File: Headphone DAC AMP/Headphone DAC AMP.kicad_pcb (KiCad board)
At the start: 4 copper layers, 95 parts, among them J1 2137160001, J2 M50-3551042, J4 PINHD_1x2_Male, U1 NCV8187AMTW090TAG, U11 ADP5071AREZ-R7, U2 XU316-1024-QF60B-C24, U6 MCP1727-1802xSN, U7 MCP1727-3302xSN, U8 W25Q16JVSNIQ, Y1 Crystal_GND24, Y2 LMK6CE049152CDLFR, Y3 ASDLJ-E-45.1584MHz

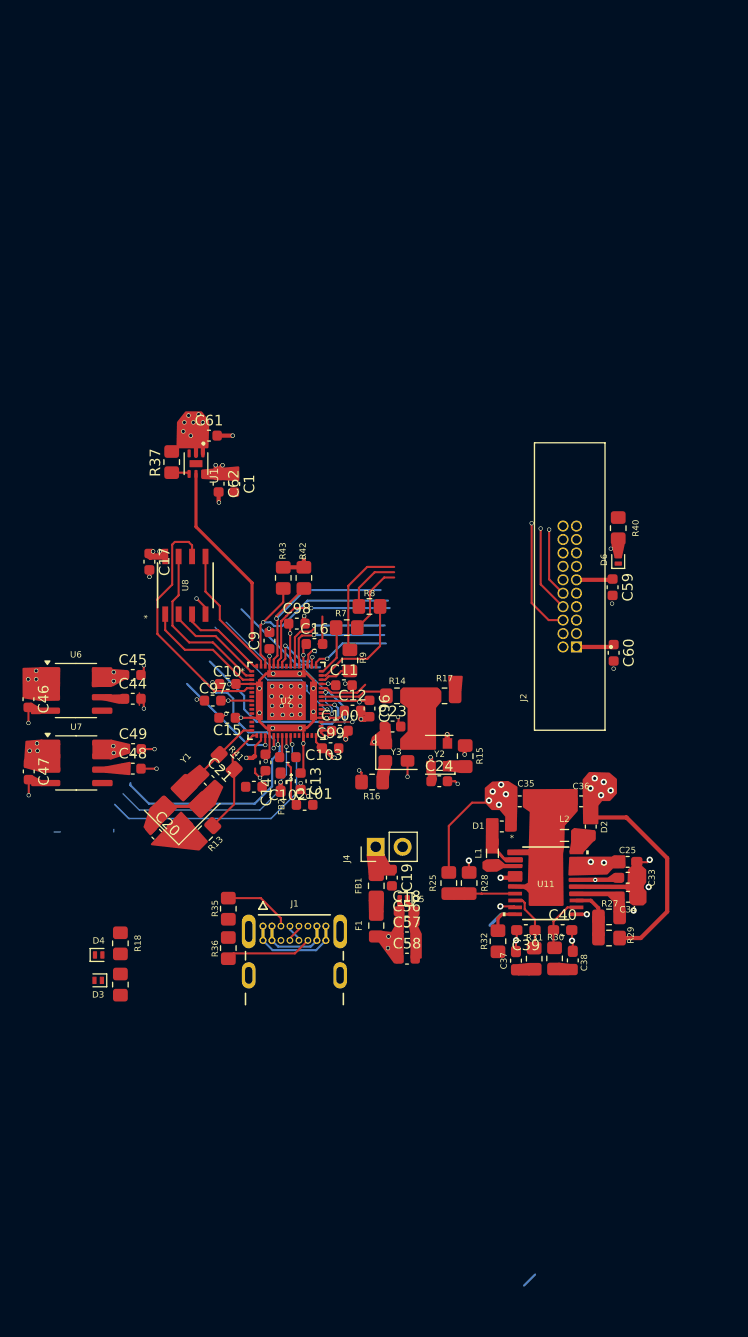
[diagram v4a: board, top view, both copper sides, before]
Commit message: Added the Board layout and castellated pins
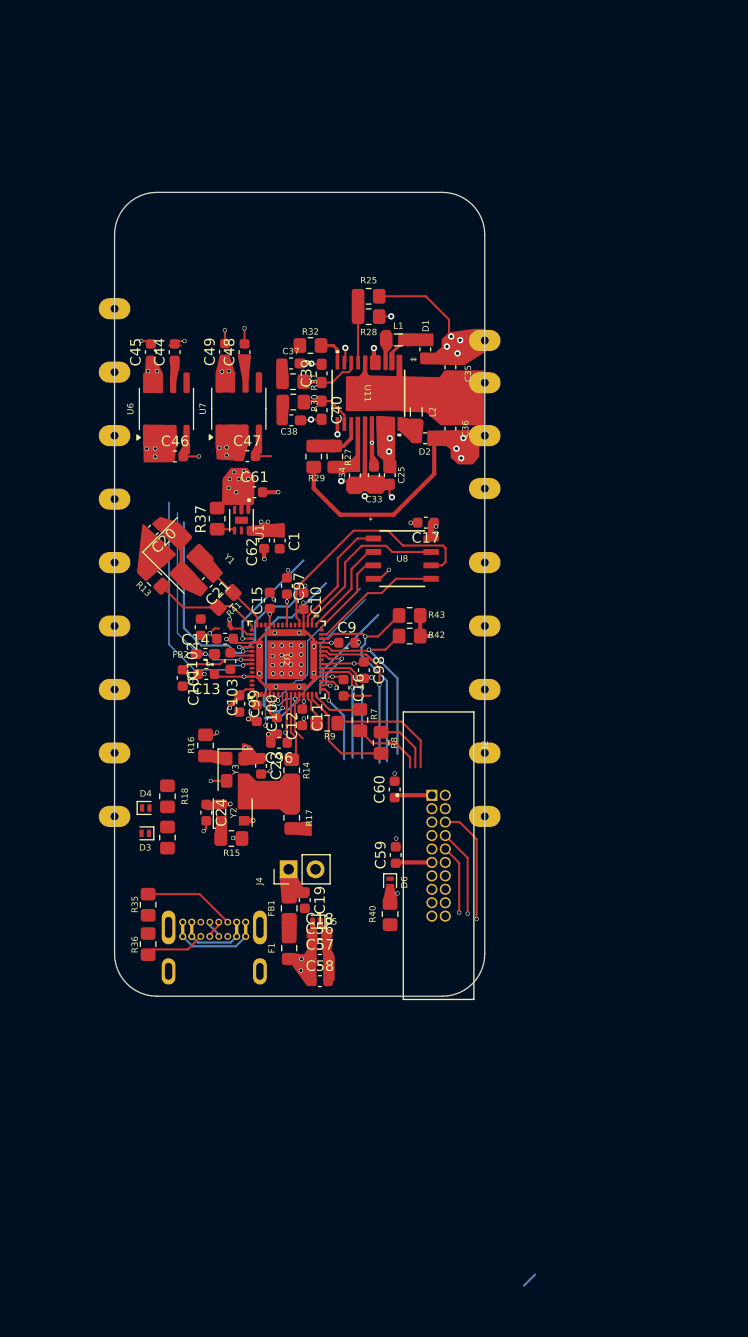
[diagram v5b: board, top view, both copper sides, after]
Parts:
- added REF**: Castellated Pin, XMOS dev board:Castellated Pin, F.Cu at (115.8, 101.9)
- added REF**: Castellated Pin, XMOS dev board:Castellated Pin, F.Cu at (80.8, 126.9)
- added REF**: Castellated Pin, XMOS dev board:Castellated Pin, F.Cu at (115.8, 108.9)
- added REF**: Castellated Pin, XMOS dev board:Castellated Pin, F.Cu at (115.8, 87.9)
- added REF**: Castellated Pin, XMOS dev board:Castellated Pin, F.Cu at (115.8, 126.9)
- added REF**: Castellated Pin, XMOS dev board:Castellated Pin, F.Cu at (115.8, 114.9)
- added REF**: Castellated Pin, XMOS dev board:Castellated Pin, F.Cu at (115.8, 91.9)
- added REF**: Castellated Pin, XMOS dev board:Castellated Pin, F.Cu at (80.8, 90.9)
- added REF**: Castellated Pin, XMOS dev board:Castellated Pin, F.Cu at (80.8, 114.9)
- added REF**: Castellated Pin, XMOS dev board:Castellated Pin, F.Cu at (80.8, 120.9)
- added REF**: Castellated Pin, XMOS dev board:Castellated Pin, F.Cu at (80.8, 108.9)
- added REF**: Castellated Pin, XMOS dev board:Castellated Pin, F.Cu at (115.8, 96.9)
- added REF**: Castellated Pin, XMOS dev board:Castellated Pin, F.Cu at (115.8, 120.9)
- added REF**: Castellated Pin, XMOS dev board:Castellated Pin, F.Cu at (115.8, 132.9)
- added REF**: Castellated Pin, XMOS dev board:Castellated Pin, F.Cu at (80.8, 102.9)
- added REF**: Castellated Pin, XMOS dev board:Castellated Pin, F.Cu at (80.8, 84.9)
- added REF**: Castellated Pin, XMOS dev board:Castellated Pin, F.Cu at (80.8, 96.9)
- added REF**: Castellated Pin, XMOS dev board:Castellated Pin, F.Cu at (80.8, 132.9)
- J1: moved to B.Cu
- moved C37 60.3 mm to (97.5, 90.1), turned to 0 degrees
- moved R31 59.1 mm to (97.7, 91.8), turned to 180 degrees
- moved R32 59.0 mm to (99.3, 88.4), turned to 180 degrees
- moved R30 58.1 mm to (97.7, 93.7), turned to 180 degrees
- moved C38 57.6 mm to (97.5, 95.5), turned to 0 degrees
- moved C39 56.1 mm to (100.4, 91.0), turned to 90 degrees
- moved R28 56.0 mm to (104.8, 83.7), turned to 180 degrees
- moved R25 54.4 mm to (104.8, 85.7), turned to 0 degrees
- moved C40 54.2 mm to (100.4, 94.5), turned to -90 degrees
- moved R29 53.4 mm to (99.6, 98.9), turned to 90 degrees
- moved R27 50.7 mm to (101.6, 98.9), turned to 90 degrees
- moved L1 49.3 mm to (107.7, 87.9), turned to 180 degrees
- moved U11 49.3 mm to (104.8, 92.9), turned to -90 degrees
- moved C34 47.5 mm to (103.5, 100.7), turned to -90 degrees
- moved D1 45.7 mm to (110.2, 88.7), turned to 90 degrees
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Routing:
- net 0V9: track 59.3 -> 41.4 mm
- net /Debug/XMOS_NRST: track 26.9 -> 24.3 mm
- net Net-(J1-CC2): track 8.27 -> 5.69 mm
- net /Debug/TMS: track 21.5 -> 19.3 mm
- net Net-(J1-CC1): track 6.51 -> 8.62 mm
- net /Debug/TCK: track 24.4 -> 22.5 mm
- net Net-(U11-SS): track 4.42 -> 2.94 mm
- net (no net): track 2.33 -> 1.48 mm
- net /USB Audio Input/SCL: track 19.6 -> 19.0 mm
- net GND: vias 49 -> 48
- net /General Power/+6V: vias 5 -> 4
- net /General Power/-6V: vias 5 -> 3
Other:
- board outline added: 35 x 76 mm

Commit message: consolidated the castellated pins into a single footprint
landed on a pitch of 2.5mm
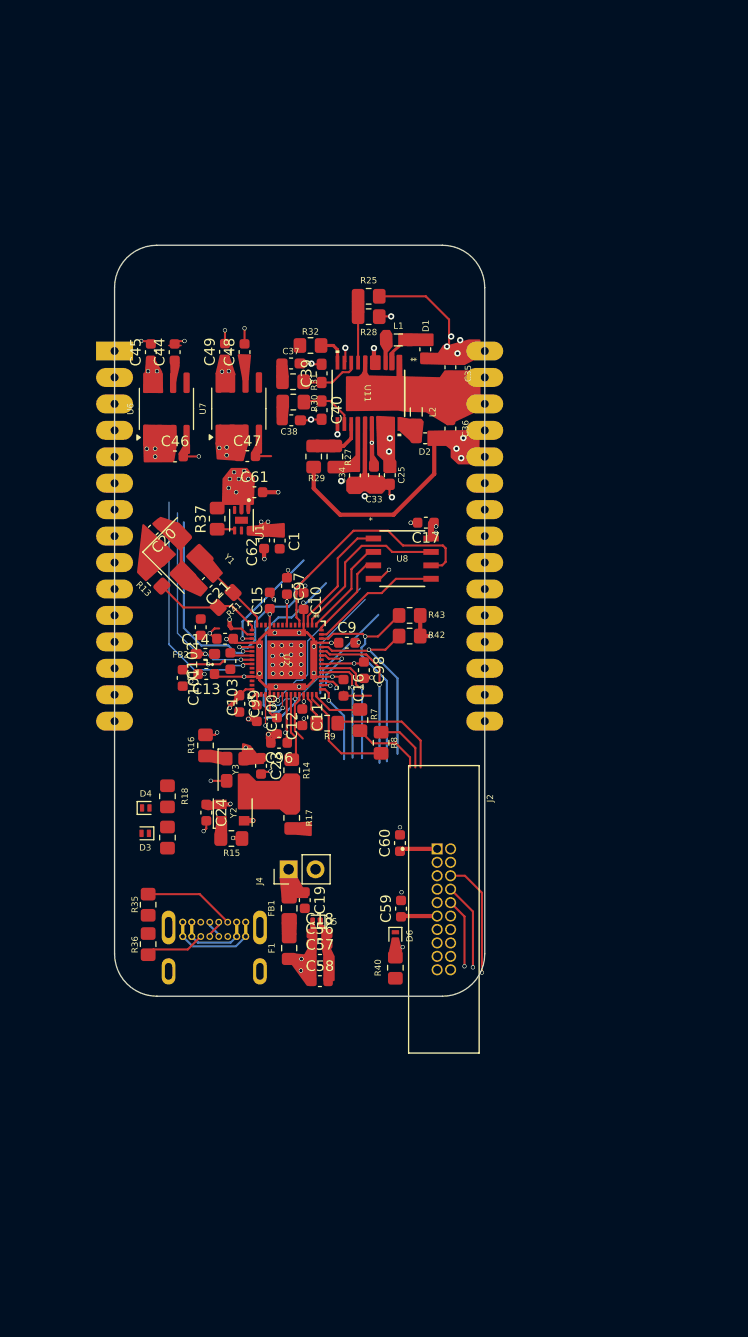
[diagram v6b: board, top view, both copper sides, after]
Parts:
- removed REF** (x18): Castellated Pin, XMOS dev board:Castellated Pin
- added B**: Castellated Pins, Library:Castellated Hole PCB, F.Cu at (98.3, 88.9)
- moved C60 5.09 mm to (107.8, 135.4)
- moved D6 5.09 mm to (107.4, 144.2)
- moved R40 5.09 mm to (107.4, 147.2)
- moved C59 5.09 mm to (107.9, 141.6)
- moved J2 5.09 mm to (112.0, 141.7)
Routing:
- net (no net): track 1.48 -> 0.00 mm
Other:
- board size 35 x 76 mm -> 35 x 71 mm

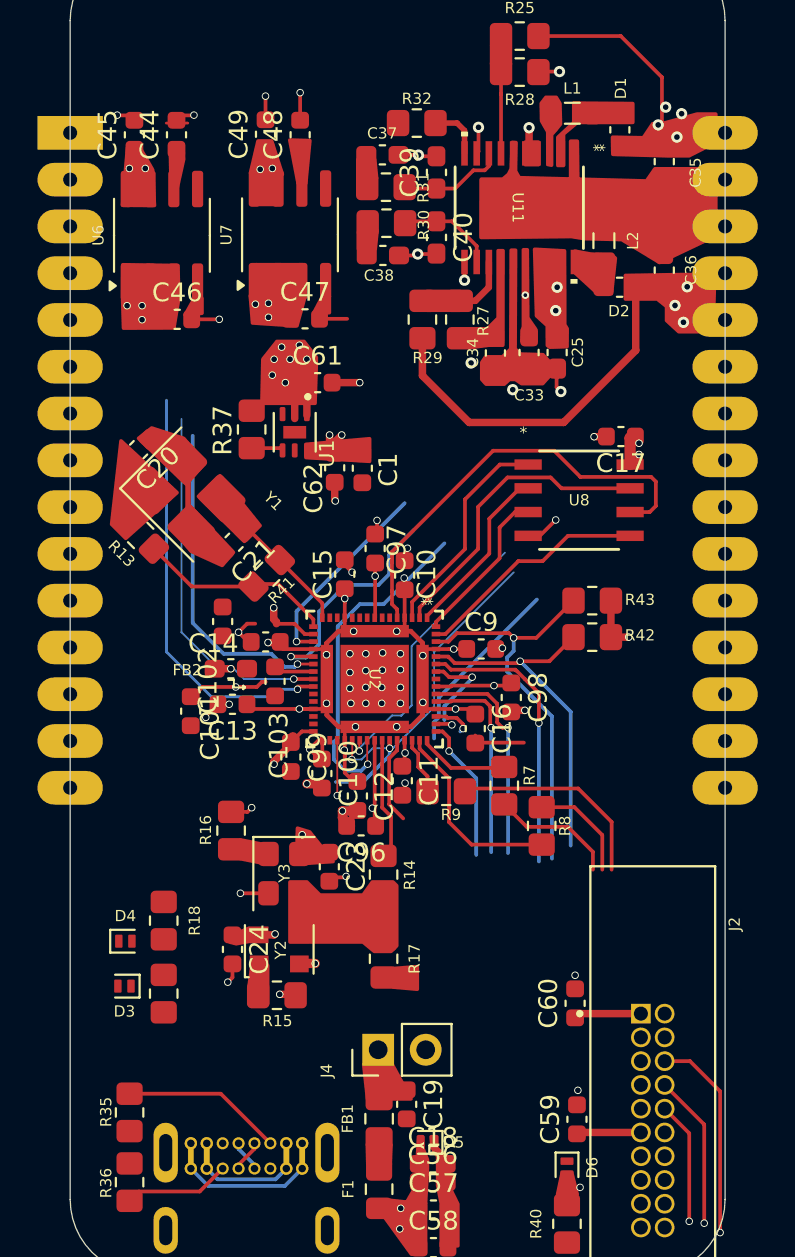
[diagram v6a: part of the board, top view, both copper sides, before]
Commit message: Finished USB D+ D- routing
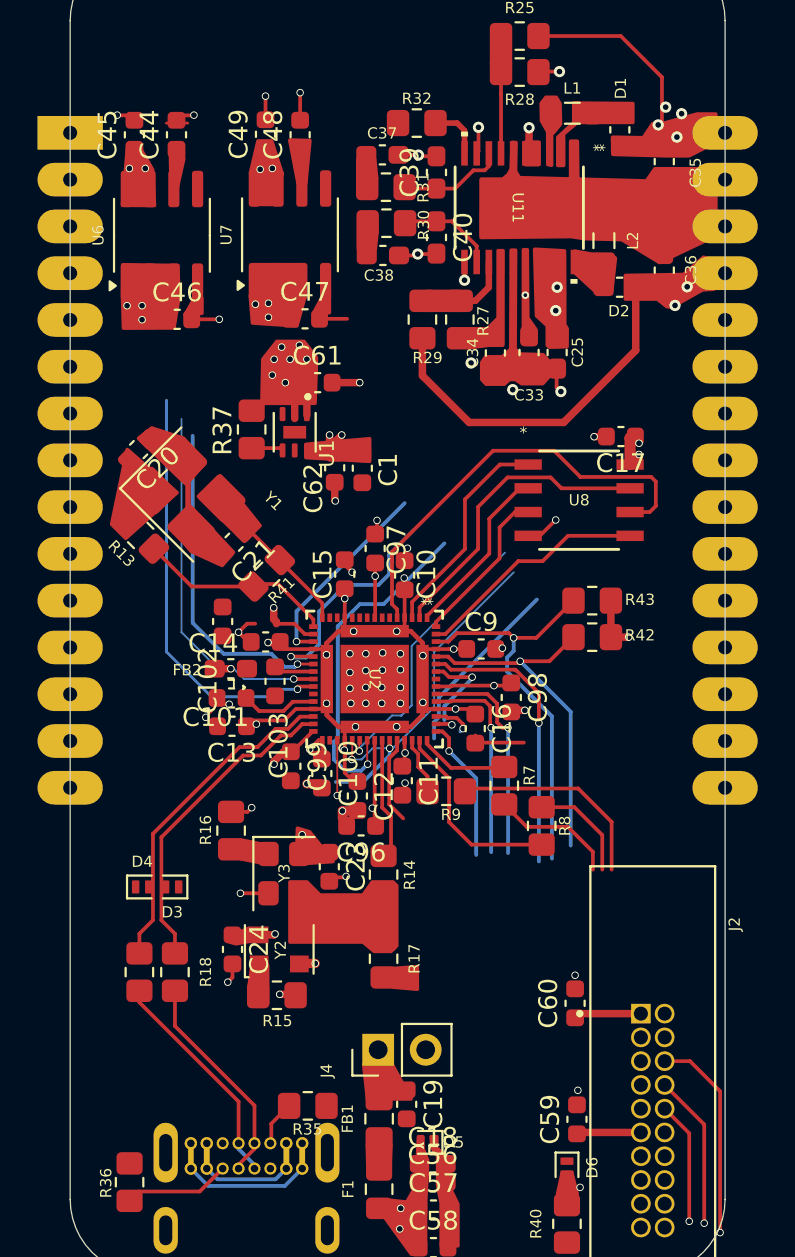
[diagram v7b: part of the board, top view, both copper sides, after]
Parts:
- moved R35 9.53 mm to (93.5, 140.9), turned to 180 degrees
- moved D3 5.88 mm to (86.3, 129.2)
- moved D4 3.04 mm to (84.7, 129.2)
- moved R18 2.81 mm to (86.4, 133.8)
- moved C101 2.29 mm to (89.5, 119.1), turned to 180 degrees
- moved R19 1.74 mm to (84.5, 133.8)
- moved C13 1.17 mm to (89.5, 120.6)
- moved C99 0.49 mm to (92.6, 122.8)
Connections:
- B** pad 16: (no net) -> /General Power/+6V
- B** pad 17: (no net) -> GND
- B** pad 18: (no net) -> GND
- B** pad 19: (no net) -> /General Power/-6V
- B** pad 8: (no net) -> GND
- B** pad 9: (no net) -> GND
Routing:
- net /USB Audio Input/D-: track 0.20 -> 18.0 mm
- net /USB Audio Input/D+: track 0.10 -> 17.1 mm
- net /USB Audio Input/PRED-: track 1.90 -> 12.2 mm
- net /USB Audio Input/PRED+: track 1.98 -> 11.9 mm
- net Net-(J1-CC1): track 8.62 -> 2.41 mm
- net 0V9: track 41.4 -> 40.7 mm
- net +3.3V: track 44.9 -> 44.5 mm, vias 17 -> 16
- net /General Power/-6V: vias 3 -> 2

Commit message: messed with the layouts a bit
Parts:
- removed J2: M50-3551042, M50_3551042:HARWIN_M50-3551042
- moved C24 14.8 mm to (103.4, 137.5), turned to 0 degrees
- moved R15 14.0 mm to (105.9, 135.1), turned to -90 degrees
- moved C60 12.0 mm to (114.8, 145.1)
- moved Y2 11.7 mm to (103.4, 135.0), turned to 180 degrees
- moved R16 10.6 mm to (96.3, 134.3)
- moved R9 10.4 mm to (111.3, 123.9)
- moved Y3 9.47 mm to (99.4, 134.7), turned to 0 degrees
- moved R7 8.79 mm to (111.3, 118.9), turned to 0 degrees
- moved C59 7.20 mm to (114.8, 139.4)
- moved R8 6.98 mm to (111.3, 121.4), turned to 0 degrees
- moved C23 6.02 mm to (99.0, 132.3), turned to 0 degrees
- moved R17 5.98 mm to (92.8, 129.4), turned to 180 degrees
- moved J4 5.11 mm to (101.6, 140.6)
- moved C11 2.01 mm to (100.1, 124.9), turned to -45 degrees
- moved D6 2.00 mm to (105.4, 144.2)
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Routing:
- net /Debug/XMOS_NRST: track 24.3 -> 1.11 mm, vias 3 -> 2
- net /Debug/TDO: track 23.4 -> 1.20 mm, vias 2 -> 1
- net /Debug/TCK: track 22.5 -> 0.85 mm
- net /Debug/TMS: track 19.3 -> 0.85 mm
- net /Debug/TDI: track 18.9 -> 0.85 mm, vias 2 -> 1
- net /Debug/4D3: track 18.3 -> 1.29 mm
- net /Debug/4D1: track 15.4 -> 0.85 mm
- net /Debug/4D2: track 14.7 -> 0.59 mm
- net /USB Audio Input/SDA: track 21.4 -> 8.26 mm
- net /USB Audio Input/DAC_GP6: track 15.1 -> 2.62 mm
- net /USB Audio Input/SCL: track 19.0 -> 7.99 mm
- net unconnected-(R9-Pad2): track 10.9 -> 0.00 mm
- net /Debug/4D0: track 12.7 -> 2.95 mm
- net /USB Audio Input/BCLK: track 3.74 -> 12.6 mm
- net /USB Audio Input/DAC_GP5: track 11.9 -> 3.24 mm
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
